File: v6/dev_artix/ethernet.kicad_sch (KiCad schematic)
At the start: 47 parts, among them J601 7499111121A, U601 KSZ9031RNXCA, Y601 KX7_QRZ_25MHz

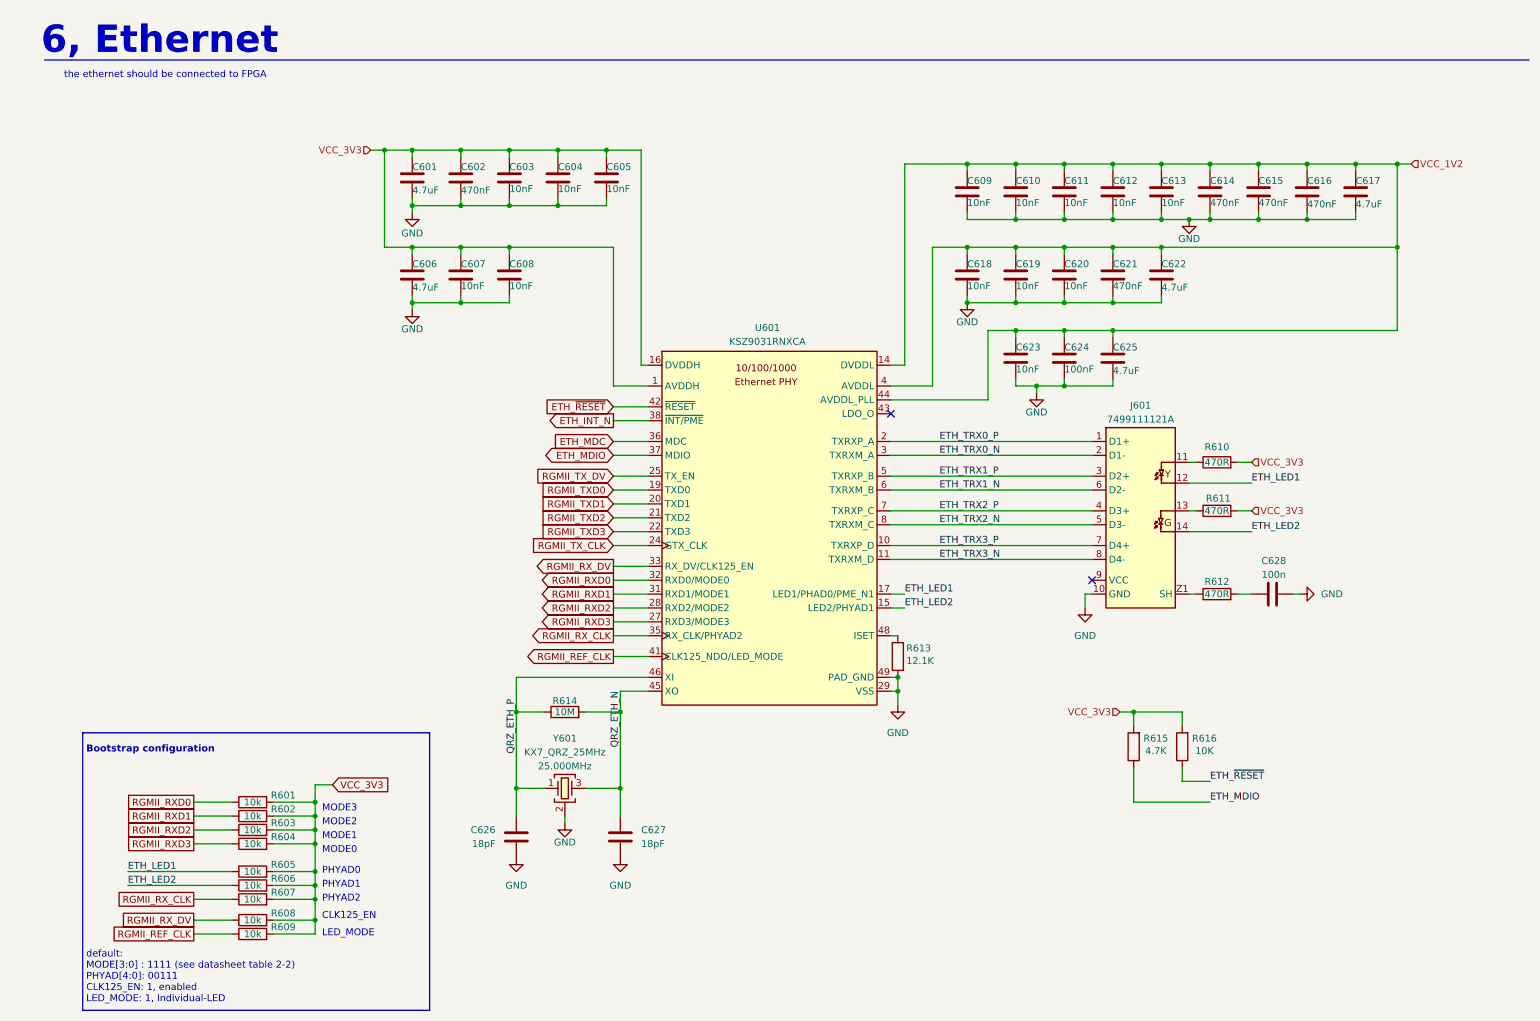
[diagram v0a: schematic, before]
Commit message: Adapt numbers for easier ordering and assembling
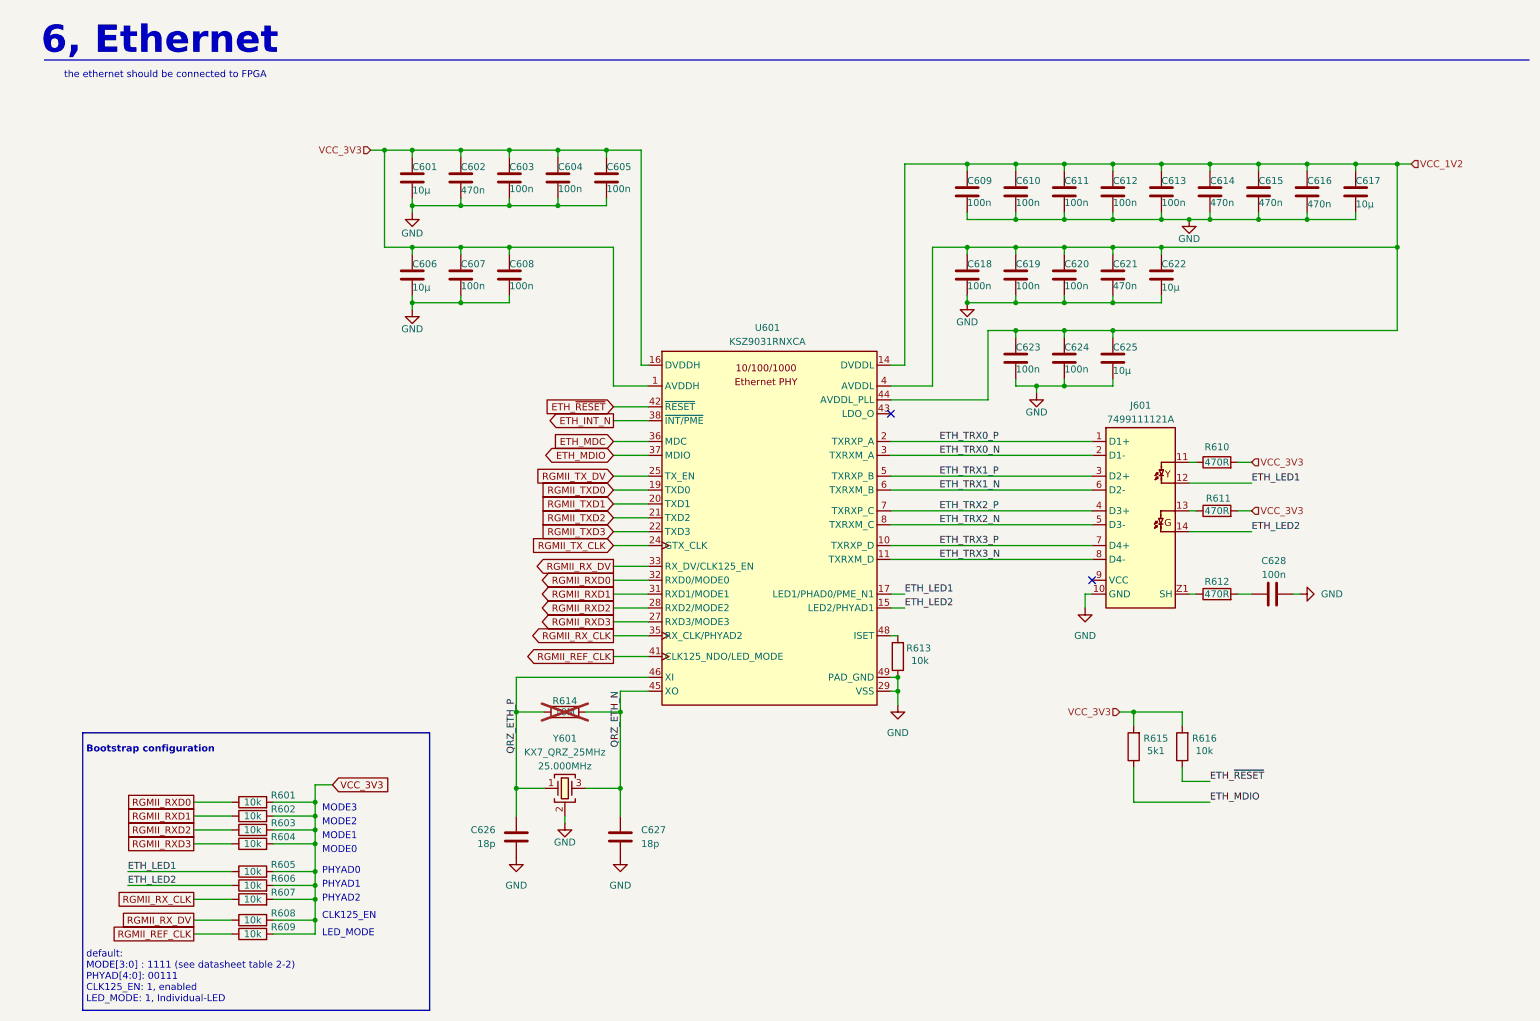
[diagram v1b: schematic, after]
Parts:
- C601, C606, C617, C622, C625: value 4.7uF -> 10µ
- C602, C614, C615, C616, C621: value 470nF -> 470n
- C603, C604, C605, C607, C608, C609, C610, C611, C612, C613, C618, C619, C620, C623: value 10nF -> 100n
- C624: value 100nF -> 100n
- C626, C627: value 18pF -> 18p
- R613: value 12.1K -> 10k
- R614: now not fitted; now left out of the parts list
- R615: value 4.7K -> 5k1
- R616: value 10K -> 10k
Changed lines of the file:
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@@
 			)
 		)
-		(property "Value" "4.7uF"
+		(property "Value" "10µ"
 			(at 252.73 45.974 0)
 			(effects
@@
 			)
 		)
-		(property "Value" "10nF"
+		(property "Value" "100n"
 			(at 181.61 45.72 0)
 			(effects
@@
 			)
 		)
-		(property "Value" "470nF"
+		(property "Value" "470n"
 			(at 208.28 60.96 0)
 			(effects
@@
 			)
 		)
-		(property "Value" "10nF"
+		(property "Value" "100n"
 			(at 217.17 45.72 0)
 			(effects
@@
 			)
 		)
-		(property "Value" "4.7uF"
+		(property "Value" "10µ"
 			(at 217.17 61.214 0)
 			(effects
@@
 			)
 		)
-		(property "Value" "4.7uF"
+		(property "Value" "10µ"
 			(at 208.28 76.454 0)
 			(effects
@@
 			)
 		)
-		(property "Value" "10nF"
+		(property "Value" "100n"
 			(at 181.61 60.96 0)
 			(effects
@@
 			)
 		)
-		(property "Value" "470nF"
+		(property "Value" "470n"
 			(at 234.95 45.72 0)
 			(effects
@@
 			)
 		)
-		(property "Value" "10nF"
+		(property "Value" "100n"
 			(at 190.5 60.96 0)
 			(effects
@@
 			)
 		)
-		(property "Value" "10K"
+		(property "Value" "10k"
 			(at 225.044 146.812 0)
 			(effects
@@
 			)
 		)
-		(property "Value" "10nF"
+		(property "Value" "100n"
 			(at 199.39 45.72 0)
 			(effects
@@
 			)
 		)
-		(property "Value" "470nF"
+		(property "Value" "470n"
 			(at 88.9 43.434 0)
 			(effects
@@
 			)
 		)
-		(property "Value" "10nF"
+		(property "Value" "100n"
 			(at 97.79 43.18 0)
 			(effects
@@
 			)
 		)
-		(property "Value" "100nF"
+		(property "Value" "100n"
 			(at 199.39 76.2 0)
 			(effects
@@
 			)
 		)
-		(property "Value" "10nF"
+		(property "Value" "100n"
 			(at 115.57 43.18 0)
 			(effects
@@
 			)
 		)
-		(property "Value" "10nF"
+		(property "Value" "100n"
 			(at 190.5 45.72 0)
 			(effects
@@
 			)
 		)
-		(property "Value" "10nF"
+		(property "Value" "100n"
 			(at 208.28 45.72 0)
 			(effects
@@
 			)
 		)
-		(property "Value" "10nF"
+		(property "Value" "100n"
 			(at 88.9 60.96 0)
 			(effects
@@
 			)
 		)
-		(property "Value" "470nF"
+		(property "Value" "470n"
 			(at 243.84 45.974 0)
 			(effects
@@
 			)
 		)
-		(property "Value" "18pF"
+		(property "Value" "18p"
 			(at 95.25 163.8299 0)
 			(effects
@@
 			)
 		)
-		(property "Value" "18pF"
+		(property "Value" "18p"
 			(at 121.92 163.8299 0)
 			(effects
@@
 			)
 		)
-		(property "Value" "4.7K"
+		(property "Value" "5k1"
 			(at 216.154 146.812 0)
 			(effects
@@
 			)
 		)
-		(property "Value" "470nF"
+		(property "Value" "470n"
 			(at 226.06 45.72 0)
 			(effects
@@
 			)
 		)
-		(property "Value" "12.1K"
+		(property "Value" "10k"
 			(at 172.974 130.302 0)
 			(effects
@@
 			)
 		)
-		(property "Value" "10nF"
+		(property "Value" "100n"
 			(at 106.68 43.18 0)
 			(effects
@@
 			)
 		)
-		(property "Value" "10nF"
+		(property "Value" "100n"
 			(at 199.39 60.96 0)
 			(effects
@@
 			)
 		)
-		(property "Value" "10nF"
+		(property "Value" "100n"
 			(at 190.5 76.2 0)
 			(effects
@@
 			)
 		)
-		(property "Value" "10nF"
+		(property "Value" "100n"
 			(at 97.79 60.96 0)
 			(effects
@@
 			)
 		)
-		(property "Value" "4.7uF"
+		(property "Value" "10µ"
 			(at 80.01 43.434 0)
 			(effects
@@
 			)
 		)
-		(property "Value" "4.7uF"
+		(property "Value" "10µ"
 			(at 80.01 61.214 0)
 			(effects
@@
 		(unit 1)
 		(exclude_from_sim no)
-		(in_bom yes)
+		(in_bom no)
 		(on_board yes)
-		(dnp no)
+		(dnp yes)
 		(property "Reference" "R614"
 			(at 107.95 137.668 90)
